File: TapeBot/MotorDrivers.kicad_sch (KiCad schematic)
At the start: 24 parts, among them J10 9652068, J3 9652068, J4 9652068, J5 9652068, J6 9652068, J7 9652068, J8 9652068, J9 9652068, U4 TB6612FNG, U5 TB6612FNG, U6 TB6612FNG, U7 TB6612FNG

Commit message: arranged board
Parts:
- C15, C16, C21, C22, C25, C26: footprint Capacitor_SMD:C_0201_0603Metric_Pad0.64x0.40mm_HandSolder -> Capacitor_SMD:C_0603_1608Metric_Pad1.08x0.95mm_HandSolder
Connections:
- net M1_CTL1: no longer U5.21 (AIN1), U6.21 (AIN1), U7.21 (AIN1)
- net M1_CTL2: no longer U5.22 (AIN2), U6.22 (AIN2), U7.22 (AIN2)
- net M1_PWM: no longer U5.23 (PWMA), U6.23 (PWMA), U7.23 (PWMA)
- net M2_CTL1: no longer U5.17 (BIN1), U6.17 (BIN1), U7.17 (BIN1)
- net M2_CTL2: no longer U5.16 (BIN2), U6.16 (BIN2), U7.16 (BIN2)
- net M2_PWM: no longer U5.15 (PWMB), U6.15 (PWMB), U7.15 (PWMB)
- removed net A01: J3.3, J5.3, J7.3, J9.3, U4.1 (A01@1), U4.2 (A01@2), U5.1 (A01@1), U5.2 (A01@2), U6.1 (A01@1), U6.2 (A01@2), U7.1 (A01@1), U7.2 (A01@2)
- removed net A02: J3.2, J5.2, J7.2, J9.2, U4.5 (A02@5), U4.6 (A02@6), U5.5 (A02@5), U5.6 (A02@6), U6.5 (A02@5), U6.6 (A02@6), U7.5 (A02@5), U7.6 (A02@6)
- removed net B01: J10.3, J4.3, J6.3, J8.3, U4.11 (B01@11), U4.12 (B01@12), U5.11 (B01@11), U5.12 (B01@12), U6.11 (B01@11), U6.12 (B01@12), U7.11 (B01@11), U7.12 (B01@12)
- removed net B02: J10.2, J4.2, J6.2, J8.2, U4.7 (B02@7), U4.8 (B02@8), U5.7 (B02@7), U5.8 (B02@8), U6.7 (B02@7), U6.8 (B02@8), U7.7 (B02@7), U7.8 (B02@8)
- new net 1A01: J3.3, U4.1 (A01@1), U4.2 (A01@2)
- new net 1A02: J3.2, U4.5 (A02@5), U4.6 (A02@6)
- new net 2B01: J4.3, U4.11 (B01@11), U4.12 (B01@12)
- new net 2B02: J4.2, U4.7 (B02@7), U4.8 (B02@8)
- new net 3A01: J7.3, U6.1 (A01@1), U6.2 (A01@2)
- new net 3A02: J7.2, U6.5 (A02@5), U6.6 (A02@6)
- new net 4B01: J8.3, U6.11 (B01@11), U6.12 (B01@12)
- new net 4B02: J8.2, U6.7 (B02@7), U6.8 (B02@8)
- new net 5A01: J5.3, U5.1 (A01@1), U5.2 (A01@2)
- new net 5A02: J5.2, U5.5 (A02@5), U5.6 (A02@6)
- new net 6B01: J6.3, U5.11 (B01@11), U5.12 (B01@12)
- new net 6B02: J6.2, U5.7 (B02@7), U5.8 (B02@8)
- new net 7A01: J9.3, U7.1 (A01@1), U7.2 (A01@2)
- new net 7A02: J9.2, U7.5 (A02@5), U7.6 (A02@6)
- new net 8B01: J10.3, U7.11 (B01@11), U7.12 (B01@12)
- new net 8B02: J10.2, U7.7 (B02@7), U7.8 (B02@8)
- new net M3_CTL1: U6.21 (AIN1)
- new net M3_CTL2: U6.22 (AIN2)
- new net M3_PWM: U6.23 (PWMA)
- new net M4_CTL1: U6.17 (BIN1)
- new net M4_CTL2: U6.16 (BIN2)
- new net M4_PWM: U6.15 (PWMB)
- new net M5_CTL1: U5.21 (AIN1)
- new net M5_CTL2: U5.22 (AIN2)
- new net M5_PWM: U5.23 (PWMA)
- new net M6_CTL1: U5.17 (BIN1)
- new net M6_CTL2: U5.16 (BIN2)
- new net M6_PWM: U5.15 (PWMB)
- new net M7_CTL1: U7.21 (AIN1)
- new net M7_CTL2: U7.22 (AIN2)
- new net M7_PWM: U7.23 (PWMA)
- new net M8_CTL1: U7.17 (BIN1)
- new net M8_CTL2: U7.16 (BIN2)
- new net M8_PWM: U7.15 (PWMB)

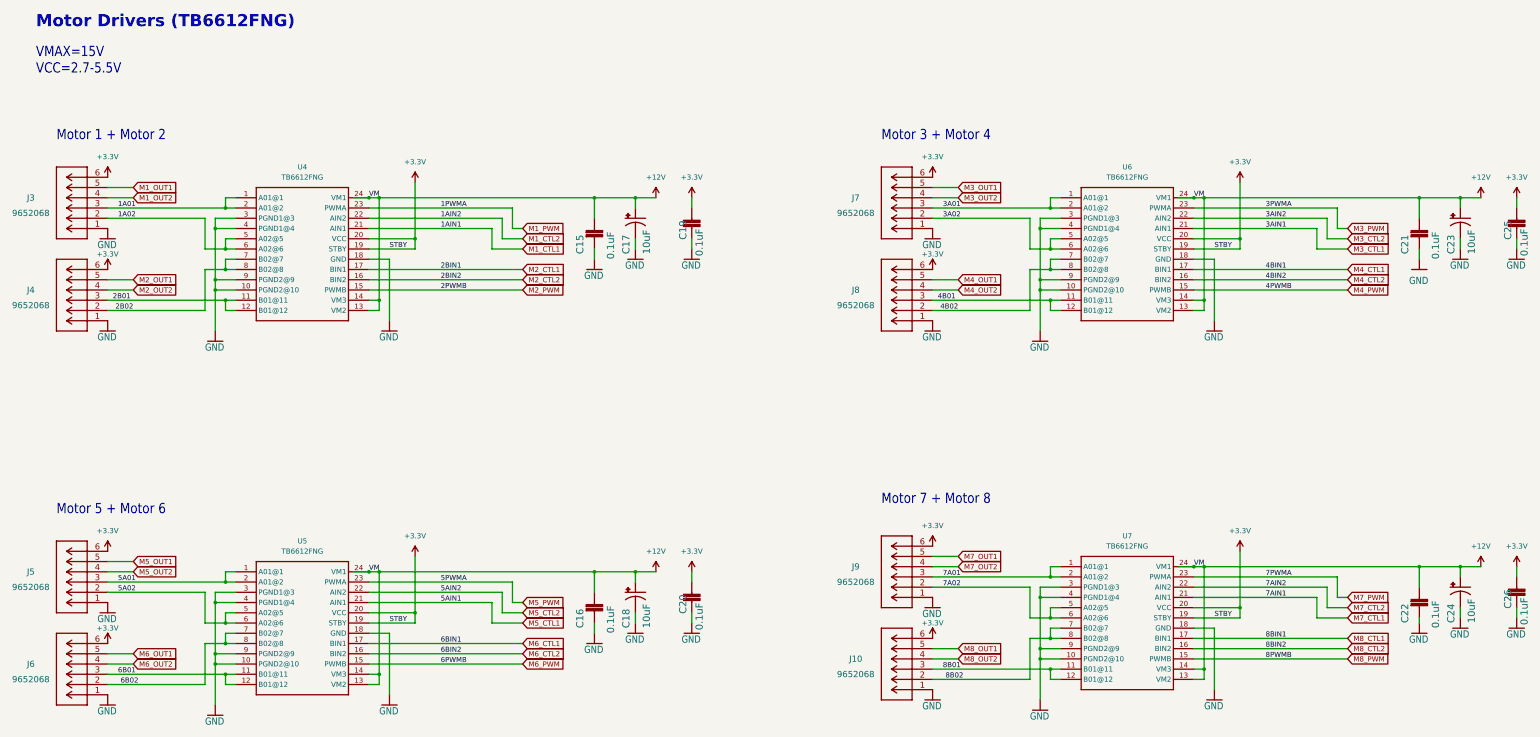
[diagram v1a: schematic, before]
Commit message: First layout of PCB finished
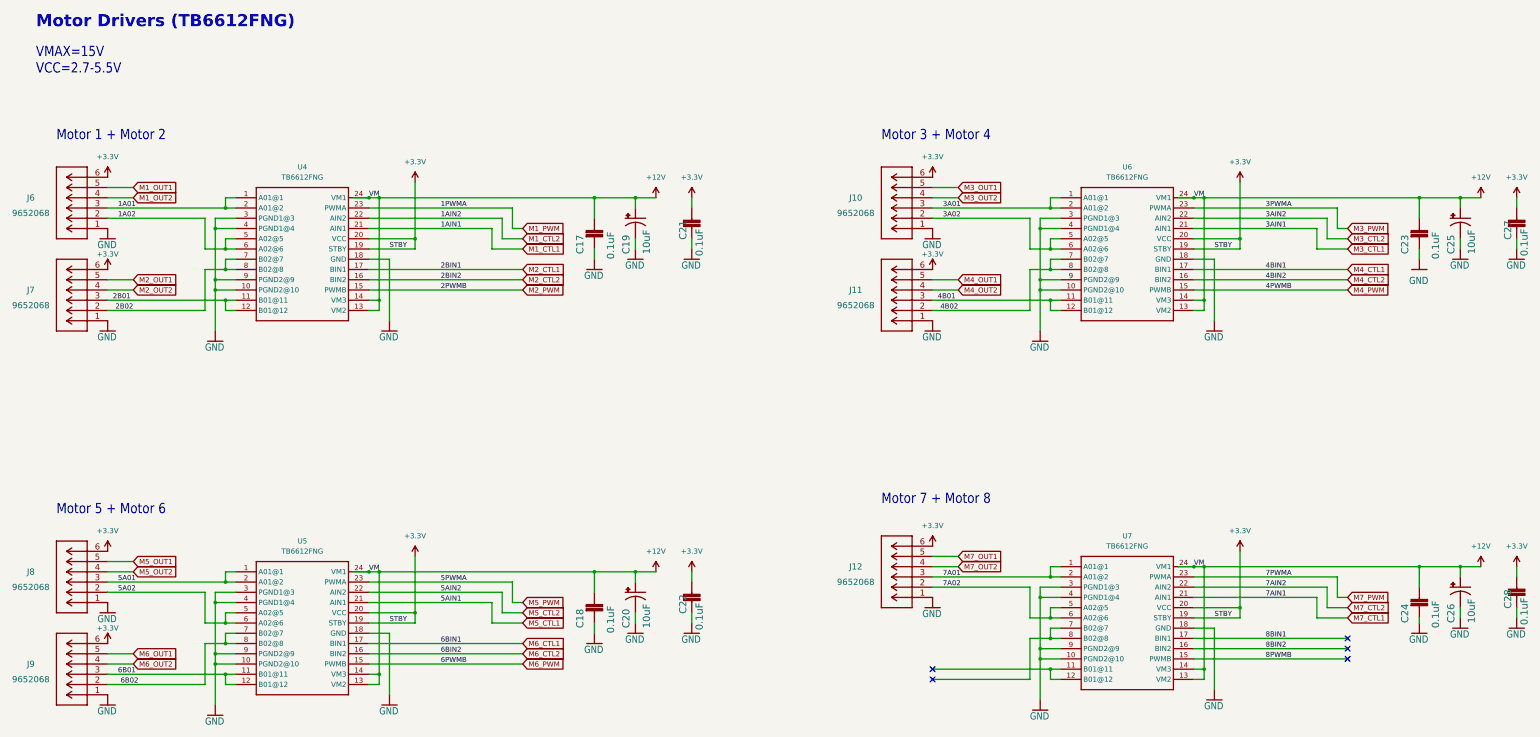
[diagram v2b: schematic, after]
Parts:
- removed J10: 9652068, tapebot:9652068, symbol tapebot:9652068
- renumbered C15 to C17, C16 to C18, C17 to C19, C18 to C20, C19 to C21, C20 to C22, C21 to C23, C22 to C24, C23 to C25, C24 to C26, C25 to C27, C26 to C28, J7 to J10, J8 to J11, J9 to J12, J3 to J6, J4 to J7, J5 to J8, J6 to J9
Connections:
- net 8B01: no longer names the net of U7.11 (B01@11), U7.12 (B01@12)
- net 8B02: no longer names the net of U7.7 (B02@7), U7.8 (B02@8)
- net M8_CTL1 renamed 8BIN1
- net M8_CTL2 renamed 8BIN2
- net M8_PWM renamed 8PWMB
- no-connect marks 0 -> 5
